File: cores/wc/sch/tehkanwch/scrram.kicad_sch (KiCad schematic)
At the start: 22 parts

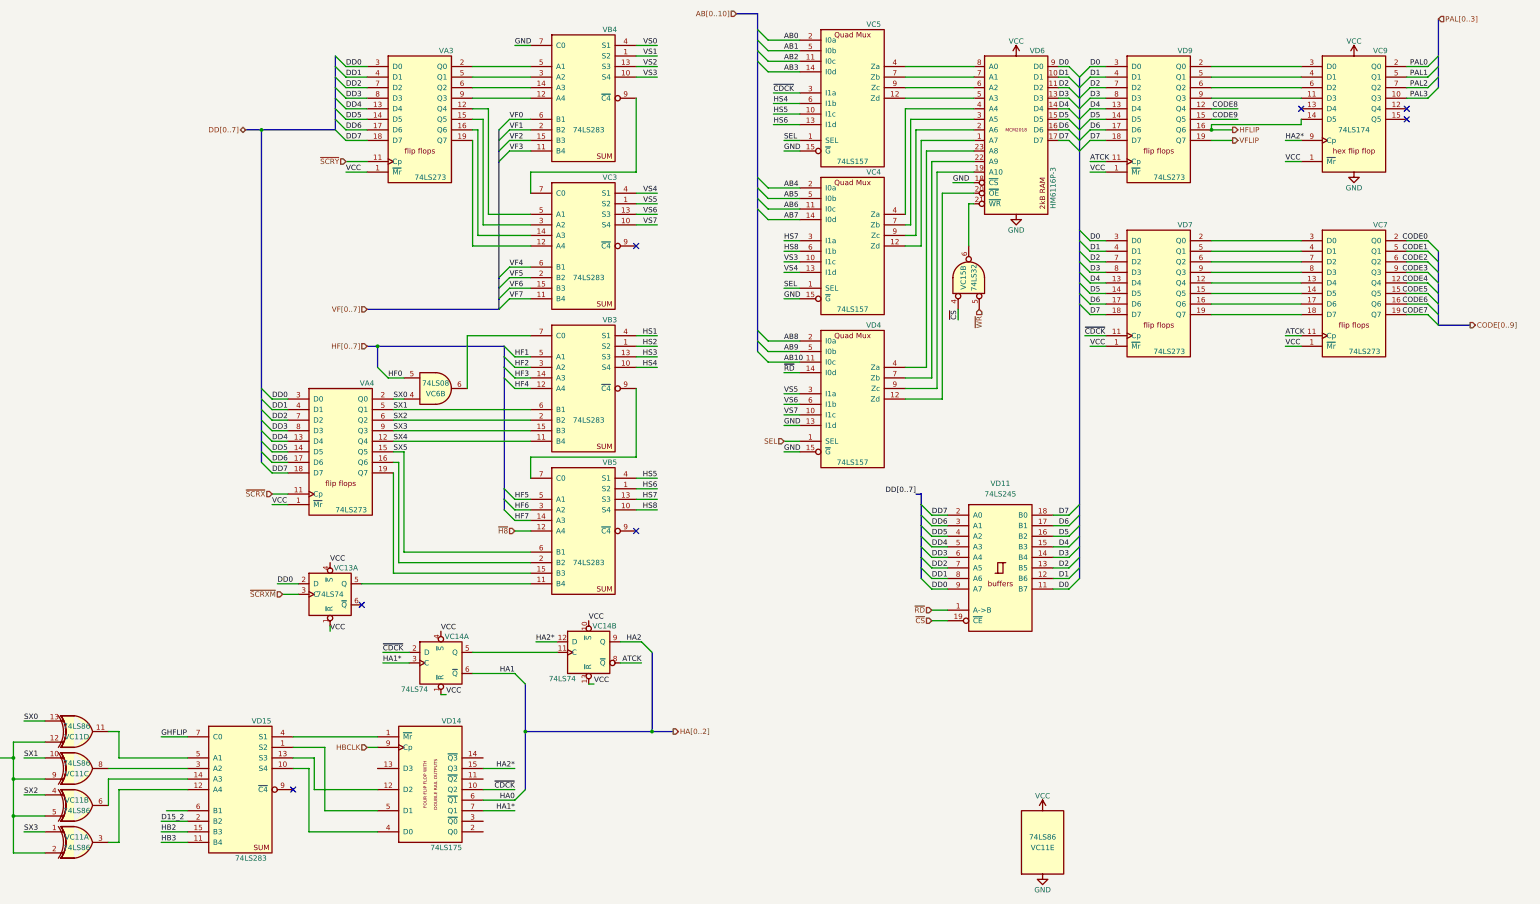
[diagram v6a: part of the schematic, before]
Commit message: wc: support for analog gamepad
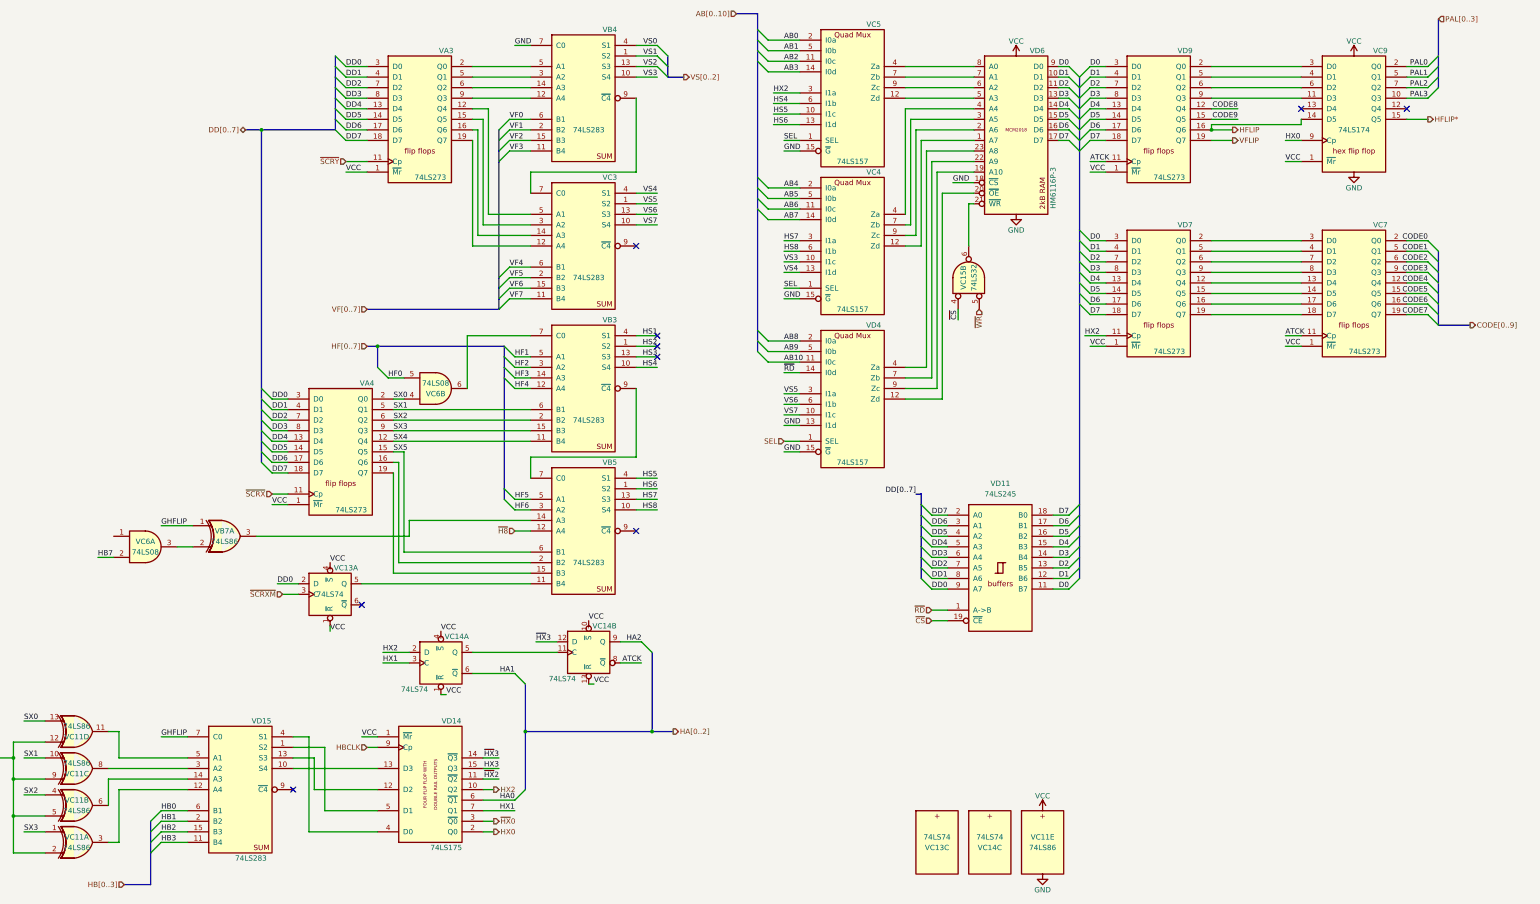
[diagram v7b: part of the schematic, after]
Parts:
- added VB7: 74LS86, symbol jt74:74LS86
- added unit 3 of VC13
- added unit 3 of VC14
- added unit 1 of VC6
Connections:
- net GHFLIP: now also VB7.1
- net GND: now also VC13.7 (VSS), VC14.7 (VSS); no longer VA3.1 (~{Mr}), VA4.1 (~{Mr}), VC11.14 (VCC), VC13.1 (~{R}), VC13.4 (~{S}), VC14.1 (~{R}), VC14.10 (~{S}), VC14.13 (~{R}), VC14.4 (~{S}), VC7.1 (~{Mr}), VC9.1 (~{Mr}), VC9.16 (VCC), VD6.24 (VCC), VD7.1 (~{Mr}), VD9.1 (~{Mr})
- net at VD15.4 (S1): now also VD14.4 (D0); no longer VD14.1 (~{Mr})
- net ~{HX}2: now reaches VD14.11 (~{Q2})
- net at VD14.13 (D3): now also VD15.10 (S4)
- net ~{HX}3: now reaches VD14.14 (~{Q3})
- net ~{HX}3: now also VC14.12 (D)
- net HX0: now reaches VD14.2 (Q0)
- net HX0: now also VC9.9 (Cp)
- net ~{HX}0: now reaches VD14.3 (~{Q0})
- net HFLIP*: now reaches VC9.15 (Q5)
- net HB0: now reaches VD15.6 (B1)
- net D15_2 renamed HB1
- net HA1* renamed HX1
- removed net HA2*: VC14.12 (D), VC9.9 (Cp), VD14.15 (Q3)
- net HF7: no longer names the net of VB5.14 (A3)
- net HF7: now also VB7.3
- net ~{CDCK} renamed HX2
- new net: VB7.2, VC6.3
- new net HB7: VC6.2
- new net HX3: VD14.15 (Q3)
- new net VCC: VA3.1 (~{Mr}), VA4.1 (~{Mr}), VC11.14 (VCC), VC13.1 (~{R}), VC13.14 (VCC), VC13.4 (~{S}), VC14.1 (~{R}), VC14.10 (~{S}), VC14.13 (~{R}), VC14.14 (VCC), VC14.4 (~{S}), VC7.1 (~{Mr}), VC9.1 (~{Mr}), VC9.16 (VCC), VD14.1 (~{Mr}), VD6.24 (VCC), VD7.1 (~{Mr}), VD9.1 (~{Mr})
- no-connect marks 7 -> 9
